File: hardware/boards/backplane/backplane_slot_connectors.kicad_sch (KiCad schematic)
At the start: 30 parts, among them J2 SLOT_4, J3 SLOT_1, J4 SLOT_2, J5 SLOT_5, J6 SLOT_6, J7 SLOT_3

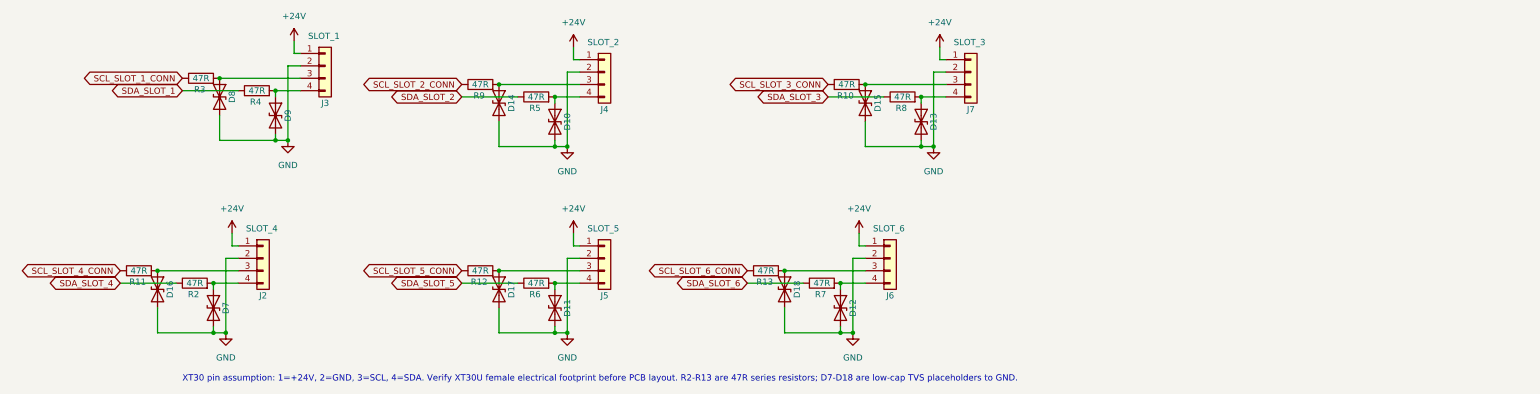
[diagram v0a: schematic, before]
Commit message: Split controller hardware from backplane
Add the central controller KiCad project for the WT32 and fan circuit, retain the I2C mux on the backplane, and update the system/interface documentation. Use C7519 arrays for interim slot I2C protection and record assembly-part alternatives.
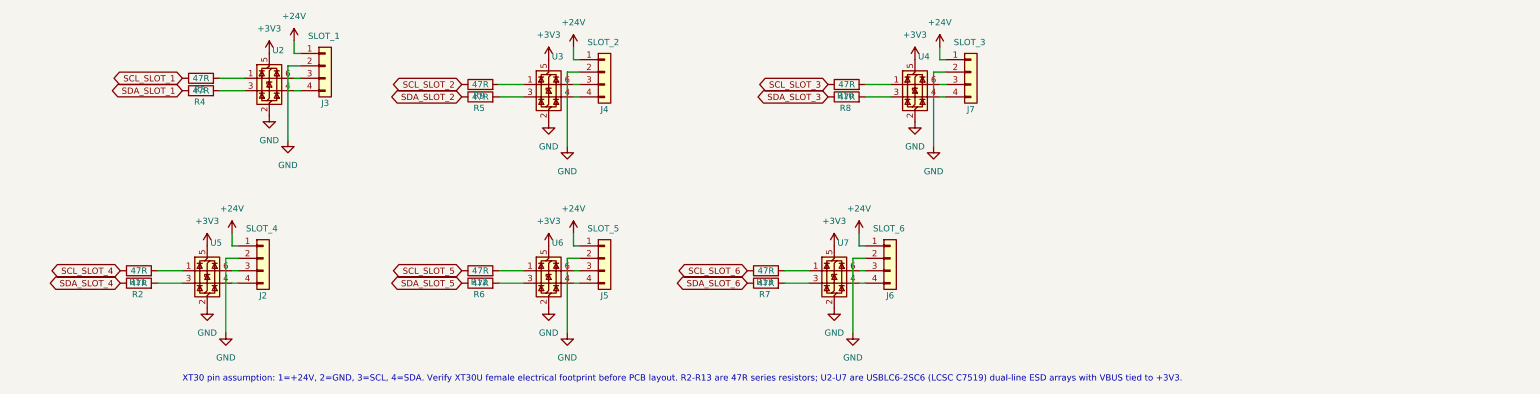
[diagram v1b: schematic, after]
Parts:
- removed D10, D11, D12, D13, D14, D15, D16, D17, D18, D7, D8, D9: LOW_CAP_TVS, Diode_SMD:D_SOD-523, symbol Device:D_TVS
- added U2, U3, U4, U5, U6, U7: USBLC6-2SC6, Package_TO_SOT_SMD:SOT-23-6, symbol Power_Protection:USBLC6-2SC6
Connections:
- net GND: now also U2.2 (GND), U3.2 (GND), U4.2 (GND), U5.2 (GND), U6.2 (GND), U7.2 (GND)
- net at R10.2: now also U4.1 (I/O1); no longer J7.3 (Pin_3)
- net at R6.2: now also U6.3 (I/O2); no longer J5.4 (Pin_4)
- net at J6.4 (Pin_4): now also U7.4 (I/O2); no longer R7.2
- net at R12.2: now also U6.1 (I/O1); no longer J5.3 (Pin_3)
- net at R4.2: now also U2.3 (I/O2); no longer J3.4 (Pin_4)
- net at R3.2: now also U2.1 (I/O1); no longer J3.3 (Pin_3)
- net at J6.3 (Pin_3): now also U7.6 (I/O1); no longer R13.2
- net at R2.2: now also U5.3 (I/O2); no longer J2.4 (Pin_4)
- net at J4.3 (Pin_3): now also U3.6 (I/O1); no longer R9.2
- net at J4.4 (Pin_4): now also U3.4 (I/O2); no longer R5.2
- net at R8.2: now also U4.3 (I/O2); no longer J7.4 (Pin_4)
- net at R11.2: now also U5.1 (I/O1); no longer J2.3 (Pin_3)
- net SCL_SLOT_1_CONN renamed SCL_SLOT_1
- net SCL_SLOT_2_CONN renamed SCL_SLOT_2
- net SCL_SLOT_3_CONN renamed SCL_SLOT_3
- net SCL_SLOT_4_CONN renamed SCL_SLOT_4
- net SCL_SLOT_5_CONN renamed SCL_SLOT_5
- net SCL_SLOT_6_CONN renamed SCL_SLOT_6
- new net: R7.2, U7.3 (I/O2)
- new net: J3.3 (Pin_3), U2.6 (I/O1)
- new net: J3.4 (Pin_4), U2.4 (I/O2)
- new net: R9.2, U3.1 (I/O1)
- new net: R5.2, U3.3 (I/O2)
- new net: R13.2, U7.1 (I/O1)
- new net: J7.4 (Pin_4), U4.4 (I/O2)
- new net: J7.3 (Pin_3), U4.6 (I/O1)
- new net: J2.4 (Pin_4), U5.4 (I/O2)
- new net: J2.3 (Pin_3), U5.6 (I/O1)
- new net: J5.4 (Pin_4), U6.4 (I/O2)
- new net: J5.3 (Pin_3), U6.6 (I/O1)
- new net +3V3: U2.5 (VBUS), U3.5 (VBUS), U4.5 (VBUS), U5.5 (VBUS), U6.5 (VBUS), U7.5 (VBUS)
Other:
- note added: "XT30 pin assumption: 1=+24V, 2=GND, 3=SCL, 4=SDA. Verify XT30U female electrical footprint before PCB layout. R2-R13 are 47R series resistors; U2-U7 are USBLC6-2SC6 (LCSC C7519) dual-line ESD arrays with VBUS tied to +3V3."
- note removed: "XT30 pin assumption: 1=+24V, 2=GND, 3=SCL, 4=SDA. Verify XT30U female electrical footprint before PCB layout. R2-R13 are 47R series resistors; D7-D18 are low-cap TVS placeholders to GND."
- moved on the sheet: R2, R4, R5, R6, R7, R8
